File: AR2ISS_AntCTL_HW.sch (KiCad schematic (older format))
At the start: 2 parts

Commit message: started schematic
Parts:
- removed U?: STM32L522CCTx, Package_QFP:LQFP-48_7x7mm_P0.5mm, symbol AR2ISS:STM32L522CCTx
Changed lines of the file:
@@
 $Descr A4 11693 8268
 encoding utf-8
-Sheet 1 1
+Sheet 1 4
 Title ""
 Date ""
@@
 Comment4 ""
 $EndDescr
-$Comp
-L AR2ISS:STM32L522CCTx U?
-U 1 1 60612BC0
-P 5150 3100
-F 0 "U?" H 5150 1511 50  0000 C CNN
-F 1 "STM32L522CCTx" H 5150 1420 50  0000 C CNN
-F 2 "Package_QFP:LQFP-48_7x7mm_P0.5mm" H 4650 1700 50  0001 R CNN
-F 3 "http://www.st.com/st-web-https://www.st.com/resource/en/datasheet/stm32l552cc.pdf" H 5150 3100 50  0001 C CNN
-	1    5150 3100
-	1    0    0    -1
-$EndComp
 $Comp
 L Interface_Expansion:MCP23008-xSO U?
@@
 	1    0    0    -1
 $EndComp
+$Sheet
+S 1150 3750 900  950
+U 60660B68
+F0 "PowerSupply" 50
+F1 "PowerSupply.sch" 50
+F2 "ADC24V" I R 2050 3900 50
+F3 "ADC12V" I R 2050 4000 50
+F4 "ADCPWR" I R 2050 4100 50
+F5 "PREAMP_ON" I R 2050 4550 50
+$EndSheet
+$Sheet
+S 2550 2400 1650 2750
+U 606DDE00
+F0 "Microcontroller" 50
+F1 "Microcontroller.sch" 50
+F2 "I2C1_SCL" I R 4200 2550 50
+F3 "I2C1_SDA" I R 4200 2650 50
+F4 "I2C2_SCL" I R 4200 2800 50
+F5 "I2C2_SDA" I R 4200 2900 50
+F6 "USART1_TX" I R 4200 3100 50
+F7 "USART1_RX" I R 4200 3200 50
+F8 "SPI2_MOSI" I R 4200 3400 50
+F9 "SPI2_CLK" I R 4200 3500 50
+$EndSheet
+$Sheet
+S 5250 2550 700  950
+U 607267A8
+F0 "IOExpander" 50
+F1 "IOExpander.sch" 50
+$EndSheet
 $EndSCHEMATC

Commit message: added display pinout
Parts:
- removed U?: MCP23008-xSO, Package_SO:SOIC-18W_7.5x11.6mm_P1.27mm, symbol Interface_Expansion:MCP23008-xSO
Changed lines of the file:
@@
 $Descr A4 11693 8268
 encoding utf-8
-Sheet 1 4
+Sheet 1 6
 Title ""
 Date ""
@@
 Comment4 ""
 $EndDescr
-$Comp
-L Interface_Expansion:MCP23008-xSO U?
-U 1 1 60613912
-P 8050 2950
-F 0 "U?" H 8050 3731 50  0000 C CNN
-F 1 "MCP23008-xSO" H 8050 3640 50  0000 C CNN
-F 2 "Package_SO:SOIC-18W_7.5x11.6mm_P1.27mm" H 8050 1900 50  0001 C CNN
-F 3 "http://ww1.microchip.com/downloads/en/DeviceDoc/MCP23008-MCP23S08-Data-Sheet-20001919F.pdf" H 9350 1750 50  0001 C CNN
-	1    8050 2950
-	1    0    0    -1
-$EndComp
 $Sheet
 S 1150 3750 900  950
@@
 $EndSheet
 $Sheet
-S 5250 2550 700  950
+S 5700 2050 750  850
 U 607267A8
 F0 "IOExpander" 50
 F1 "IOExpander.sch" 50
+F2 "SDA" I L 5700 2100 50
+F3 "SCL" I L 5700 2200 50
+F4 "RESET" I L 5700 2450 50
+F5 "A0" I L 5700 2700 50
+F6 "A1" I L 5700 2800 50
+F7 "IOs" I R 6450 2250 50
 $EndSheet
+$Sheet
+S 5700 3200 750  850
+U 60679D69
+F0 "IOExpander2" 50
+F1 "IOExpander.sch" 50
+F2 "SDA" I L 5700 3250 50
+F3 "SCL" I L 5700 3350 50
+F4 "RESET" I L 5700 3600 50
+F5 "A0" I L 5700 3850 50
+F6 "A1" I L 5700 3950 50
+F7 "IOs" I R 6450 3400 50
+$EndSheet
+$Sheet
+S 6900 2000 950  2350
+U 60679DF6
+F0 "LCD" 50
+F1 "LCD.sch" 50
+F2 "ENC_A" I R 7850 2100 50
+F3 "ENC_B" I R 7850 2200 50
+F4 "DisplayData" I R 7850 2400 50
+F5 "DisplayCLK" I R 7850 2500 50
+F6 "LEDs" I L 6900 2250 50
+$EndSheet
+Wire Bus Line
+	6450 2250 6900 2250
 $EndSCHEMATC

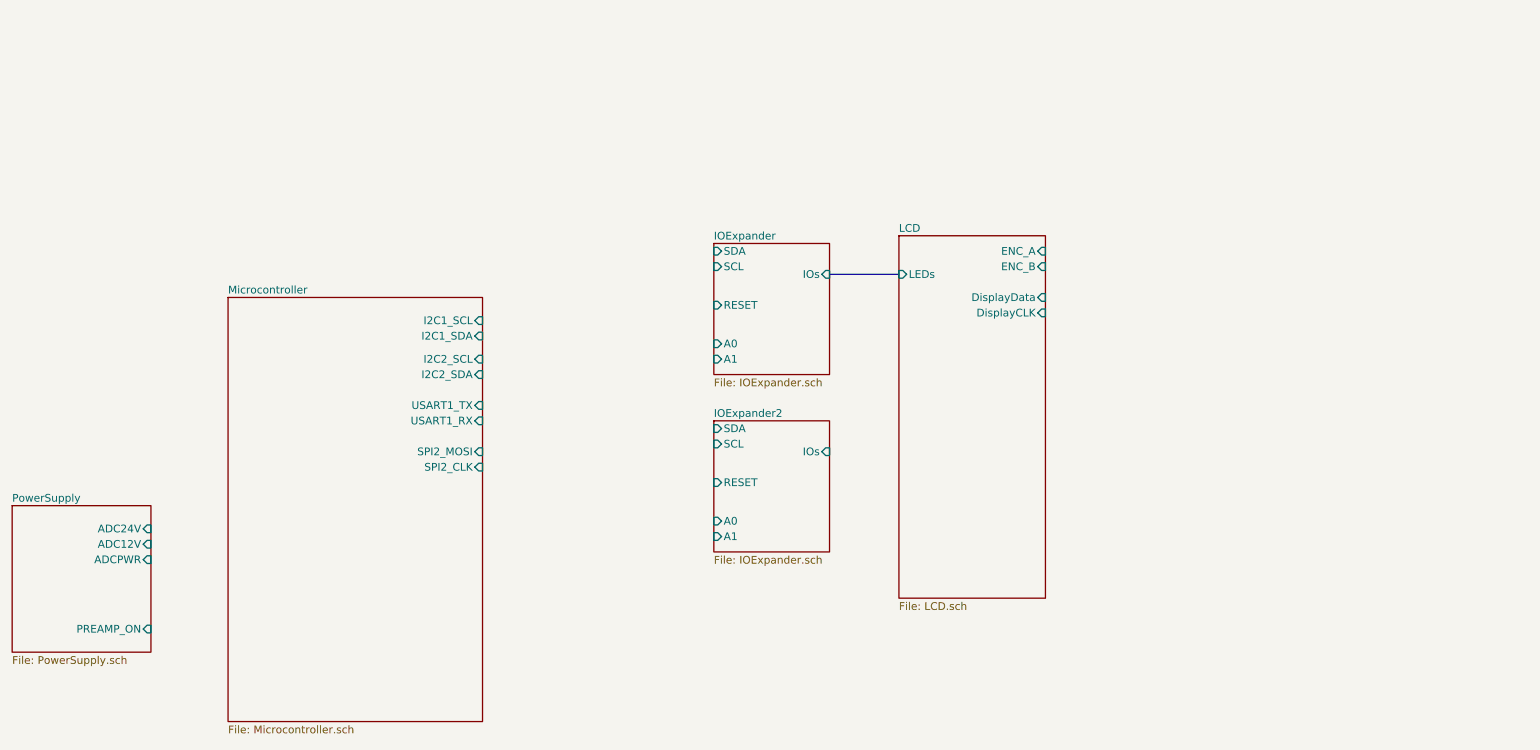
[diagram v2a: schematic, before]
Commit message: added rj45 input
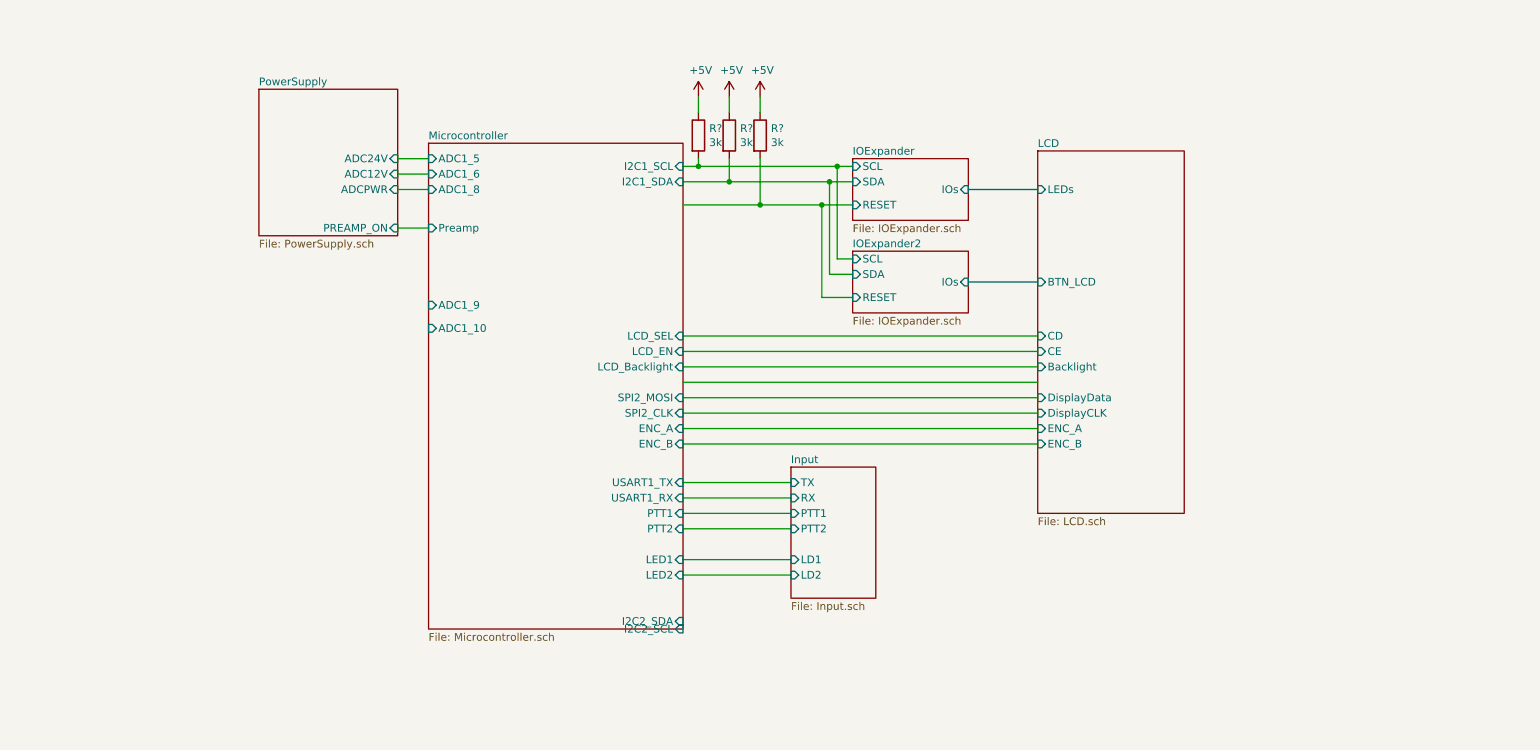
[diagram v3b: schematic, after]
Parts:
- added R? (x3): 3k, symbol AR2ISS:R
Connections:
- net labels added: +5V
- wire segments 0 -> 39

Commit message: Ready for layout
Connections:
- wire segments 39 -> 49
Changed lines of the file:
@@
 $Descr A4 11693 8268
 encoding utf-8
-Sheet 1 7
+Sheet 1 9
 Title ""
 Date ""
@@
 F4 "ADCPWR" I R 3650 1700 50
 F5 "PREAMP_ON" I R 3650 1950 50
-$EndSheet
-$Sheet
-S 3850 1400 1650 3150
-U 606DDE00
-F0 "Microcontroller" 50
-F1 "Microcontroller.sch" 50
-F2 "I2C1_SCL" I R 5500 1550 50
-F3 "I2C1_SDA" I R 5500 1650 50
-F4 "I2C2_SCL" I R 5500 4550 50
-F5 "I2C2_SDA" I R 5500 4500 50
-F6 "USART1_TX" I R 5500 3600 50
-F7 "USART1_RX" I R 5500 3700 50
-F8 "SPI2_MOSI" I R 5500 3050 50
-F9 "SPI2_CLK" I R 5500 3150 50
-F10 "LED1" I R 5500 4100 50
-F11 "LED2" I R 5500 4200 50
-F12 "ENC_A" I R 5500 3250 50
-F13 "ENC_B" I R 5500 3350 50
-F14 "PTT1" I R 5500 3800 50
-F15 "PTT2" I R 5500 3900 50
-F16 "LCD_EN" I R 5500 2750 50
-F17 "LCD_SEL" I R 5500 2650 50
-F18 "LCD_Backlight" I R 5500 2850 50
-F19 "ADC1_5" I L 3850 1500 50
-F20 "ADC1_6" I L 3850 1600 50
-F21 "ADC1_8" I L 3850 1700 50
-F22 "ADC1_9" I L 3850 2450 50
-F23 "ADC1_10" I L 3850 2600 50
-F24 "Preamp" I L 3850 1950 50
 $EndSheet
 $Sheet
@@
 Wire Wire Line
 	6000 1500 6000 1800
-Connection ~ 6000 1800
-Wire Wire Line
-	6000 1800 5500 1800
 $Comp
 L power:+5V #PWR?
@@
 Wire Wire Line
 	3650 1950 3850 1950
+$Sheet
+S 3850 1400 1650 3150
+U 606DDE00
+F0 "Microcontroller" 50
+F1 "Microcontroller.sch" 50
+F2 "I2C1_SCL" I R 5500 1550 50
+F3 "I2C1_SDA" I R 5500 1650 50
+F4 "USART1_TX" I R 5500 3600 50
+F5 "USART1_RX" I R 5500 3700 50
+F6 "SPI2_MOSI" I R 5500 3050 50
+F7 "SPI2_CLK" I R 5500 3150 50
+F8 "LED1" I R 5500 4100 50
+F9 "LED2" I R 5500 4200 50
+F10 "ENC_A" I R 5500 3250 50
+F11 "ENC_B" I R 5500 3350 50
+F12 "LCD_EN" I R 5500 2750 50
+F13 "LCD_SEL" I R 5500 2650 50
+F14 "LCD_Backlight" I R 5500 2850 50
+F15 "ADC1_5" I L 3850 1500 50
+F16 "ADC1_6" I L 3850 1600 50
+F17 "ADC1_8" I L 3850 1700 50
+F18 "ADC1_9" I L 3850 3900 50
+F19 "ADC1_10" I L 3850 4000 50
+F20 "Preamp" I L 3850 1950 50
+F21 "PTT_Main" I R 5500 3800 50
+F22 "PTT_Sub" I R 5500 3900 50
+F23 "ROT_UP" I L 3850 4150 50
+F24 "ROT_DOWN" I L 3850 4250 50
+F25 "ROT_LEFT" I L 3850 4350 50
+F26 "ROT_RIGHT" I L 3850 4450 50
+F27 "CREL_A" I L 3850 3300 50
+F28 "CREL_B" I L 3850 3200 50
+F29 "AMP" I L 3850 3000 50
+F30 "C_NO" I L 3850 2700 50
+F31 "C_NC" I L 3850 2800 50
+$EndSheet
+$Sheet
+S 2650 3850 750  950
+U 6074FD4F
+F0 "Rotor" 50
+F1 "Rotor.sch" 50
+F2 "ROT_UP" I R 3400 4150 50
+F3 "ROT_DOWN" I R 3400 4250 50
+F4 "ROT_LEFT" I R 3400 4350 50
+F5 "ROT_RIGHT" I R 3400 4450 50
+F6 "POT_ELE" I R 3400 3900 50
+F7 "POT_AZI" I R 3400 4000 50
+$EndSheet
+Wire Wire Line
+	3850 3900 3400 3900
+Wire Wire Line
+	3400 4000 3850 4000
+Wire Wire Line
+	3400 4150 3850 4150
+Wire Wire Line
+	3400 4250 3850 4250
+Wire Wire Line
+	3400 4350 3850 4350
+Wire Wire Line
+	3400 4450 3850 4450
+$Sheet
+S 2800 2600 600  800
+U 607E0323
+F0 "HF_Ctrl" 50
+F1 "HF_Ctrl.sch" 50
+F2 "AMP_ON" I R 3400 3000 50
+F3 "Coax_NO" I R 3400 2700 50
+F4 "Coax_NC" I R 3400 2800 50
+F5 "Coax_Rel_A" I R 3400 3200 50
+F6 "Coax_Ref_B" I R 3400 3300 50
+$EndSheet
+Wire Wire Line
+	3400 3000 3850 3000
+Wire Wire Line
+	3400 3200 3850 3200
+Wire Wire Line
+	3400 3300 3850 3300
+Wire Wire Line
+	3850 2700 3400 2700
+Wire Wire Line
+	3400 2800 3850 2800
 $EndSCHEMATC

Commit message: first layout
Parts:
- added U1, U2, U3, U4: non_plated, stmbl:non_plated_3mm, symbol stmbl:non_plated
- R1, R2, R3: renamed from R?; footprint (none) -> Resistor_SMD:R_0603_1608Metric
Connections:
- wire segments 49 -> 48
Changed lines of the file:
@@
 $Descr A4 11693 8268
 encoding utf-8
-Sheet 1 9
+Sheet 1 17
 Title ""
 Date ""
@@
 F0 "IOExpander2" 50
 F1 "IOExpander.sch" 50
-F2 "SDA" I L 6600 2250 50
+F2 "SDA" B L 6600 2250 50
 F3 "SCL" I L 6600 2150 50
 F4 "RESET" I L 6600 2400 50
-F5 "IOs" I R 7350 2300 50
+F5 "IO[0..15]" O R 7350 2300 50
 $EndSheet
 $Sheet
@@
 F4 "DisplayData" I L 7800 3050 50
 F5 "DisplayCLK" I L 7800 3150 50
-F6 "LEDs" I L 7800 1700 50
-F7 "BTN_LCD" I L 7800 2300 50
+F6 "LEDs[0..15]" I L 7800 1700 50
+F7 "BTN[0..15]" I L 7800 2300 50
 F8 "CD" I L 7800 2650 50
 F9 "CE" I L 7800 2750 50
@@
 AR Path="/60679D69/60A57B75" Ref="R?"  Part="1"
 AR Path="/607267A8/60A57B75" Ref="R?"  Part="1"
-AR Path="/60A57B75" Ref="R?"  Part="1"
-F 0 "R?" H 5670 1396 50  0000 L CNN
+AR Path="/60A57B75" Ref="R1"  Part="1"
+F 0 "R1" H 5670 1396 50  0000 L CNN
 F 1 "3k" H 5670 1305 50  0000 L CNN
-F 2 "" V 5530 1350 50  0001 C CNN
+F 2 "Resistor_SMD:R_0603_1608Metric" V 5530 1350 50  0001 C CNN
 F 3 "~" H 5600 1350 50  0001 C CNN
 	1    5600 1350
@@
 AR Path="/60679D69/60A57BD2" Ref="R?"  Part="1"
 AR Path="/607267A8/60A57BD2" Ref="R?"  Part="1"
-AR Path="/60A57BD2" Ref="R?"  Part="1"
-F 0 "R?" H 5870 1396 50  0000 L CNN
+AR Path="/60A57BD2" Ref="R2"  Part="1"
+F 0 "R2" H 5870 1396 50  0000 L CNN
 F 1 "3k" H 5870 1305 50  0000 L CNN
-F 2 "" V 5730 1350 50  0001 C CNN
+F 2 "Resistor_SMD:R_0603_1608Metric" V 5730 1350 50  0001 C CNN
 F 3 "~" H 5800 1350 50  0001 C CNN
 	1    5800 1350
@@
 AR Path="/607267A8/60A66FB9" Ref="#PWR?"  Part="1"
 AR Path="/60679D69/60A66FB9" Ref="#PWR?"  Part="1"
-AR Path="/60A66FB9" Ref="#PWR?"  Part="1"
-F 0 "#PWR?" H 5600 950 50  0001 C CNN
+AR Path="/60A66FB9" Ref="#PWR01"  Part="1"
+F 0 "#PWR01" H 5600 950 50  0001 C CNN
 F 1 "+5V" H 5615 1273 50  0000 C CNN
 F 2 "" H 5600 1100 50  0001 C CNN
@@
 AR Path="/607267A8/60A6763B" Ref="#PWR?"  Part="1"
 AR Path="/60679D69/60A6763B" Ref="#PWR?"  Part="1"
-AR Path="/60A6763B" Ref="#PWR?"  Part="1"
-F 0 "#PWR?" H 5800 950 50  0001 C CNN
+AR Path="/60A6763B" Ref="#PWR02"  Part="1"
+F 0 "#PWR02" H 5800 950 50  0001 C CNN
 F 1 "+5V" H 5815 1273 50  0000 C CNN
 F 2 "" H 5800 1100 50  0001 C CNN
@@
 Wire Wire Line
 	5800 1100 5800 1200
-$Sheet
-S 6200 3500 550  850
-U 60A6CF0D
-F0 "Input" 50
-F1 "Input.sch" 50
-F2 "TX" I L 6200 3600 50
-F3 "RX" I L 6200 3700 50
-F4 "PTT1" I L 6200 3800 50
-F5 "PTT2" I L 6200 3900 50
-F6 "LD1" I L 6200 4100 50
-F7 "LD2" I L 6200 4200 50
-$EndSheet
 Wire Wire Line
 	5500 3900 6200 3900
@@
 F0 "IOExpander" 50
 F1 "IOExpander.sch" 50
-F2 "SDA" I L 6600 1650 50
+F2 "SDA" B L 6600 1650 50
 F3 "SCL" I L 6600 1550 50
 F4 "RESET" I L 6600 1800 50
-F5 "IOs" I R 7350 1700 50
+F5 "IO[0..15]" O R 7350 1700 50
 $EndSheet
 Wire Wire Line
@@
 AR Path="/60679D69/60C11F73" Ref="R?"  Part="1"
 AR Path="/607267A8/60C11F73" Ref="R?"  Part="1"
-AR Path="/60C11F73" Ref="R?"  Part="1"
-F 0 "R?" H 6070 1396 50  0000 L CNN
+AR Path="/60C11F73" Ref="R3"  Part="1"
+F 0 "R3" H 6070 1396 50  0000 L CNN
 F 1 "3k" H 6070 1305 50  0000 L CNN
-F 2 "" V 5930 1350 50  0001 C CNN
+F 2 "Resistor_SMD:R_0603_1608Metric" V 5930 1350 50  0001 C CNN
 F 3 "~" H 6000 1350 50  0001 C CNN
 	1    6000 1350
@@
 AR Path="/607267A8/60C1252C" Ref="#PWR?"  Part="1"
 AR Path="/60679D69/60C1252C" Ref="#PWR?"  Part="1"
-AR Path="/60C1252C" Ref="#PWR?"  Part="1"
-F 0 "#PWR?" H 6000 950 50  0001 C CNN
+AR Path="/60C1252C" Ref="#PWR03"  Part="1"
+F 0 "#PWR03" H 6000 950 50  0001 C CNN
 F 1 "+5V" H 6015 1273 50  0000 C CNN
 F 2 "" H 6000 1100 50  0001 C CNN
@@
 	5500 2850 7800 2850
 Wire Wire Line
-	7800 2950 5500 2950
-Wire Wire Line
 	5500 3150 7800 3150
 Wire Wire Line
@@
 F0 "Microcontroller" 50
 F1 "Microcontroller.sch" 50
-F2 "I2C1_SCL" I R 5500 1550 50
-F3 "I2C1_SDA" I R 5500 1650 50
+F2 "I2C1_SCL" O R 5500 1550 50
+F3 "I2C1_SDA" B R 5500 1650 50
 F4 "USART1_TX" I R 5500 3600 50
 F5 "USART1_RX" I R 5500 3700 50
@@
 F15 "ADC1_5" I L 3850 1500 50
 F16 "ADC1_6" I L 3850 1600 50
-F17 "ADC1_8" I L 3850 1700 50
+F17 "ADC1_8" I L 3850 4000 50
 F18 "ADC1_9" I L 3850 3900 50
-F19 "ADC1_10" I L 3850 4000 50
+F19 "ADC1_10" I L 3850 1700 50
 F20 "Preamp" I L 3850 1950 50
 F21 "PTT_Main" I R 5500 3800 50
@@
 F1 "HF_Ctrl.sch" 50
 F2 "AMP_ON" I R 3400 3000 50
-F3 "Coax_NO" I R 3400 2700 50
-F4 "Coax_NC" I R 3400 2800 50
-F5 "Coax_Rel_A" I R 3400 3200 50
-F6 "Coax_Ref_B" I R 3400 3300 50
+F3 "Coax_NO" I R 3400 3300 50
+F4 "Coax_NC" I R 3400 3200 50
+F5 "Coax_Rel_A" I R 3400 2800 50
+F6 "Coax_Ref_B" I R 3400 2700 50
 $EndSheet
 Wire Wire Line
@@
 Wire Wire Line
 	3400 2800 3850 2800
+$Comp
+L stmbl:non_plated U1
+U 1 1 6070B730
+P 9350 700
+F 0 "U1" H 9528 753 60  0000 L CNN
+F 1 "non_plated" H 9528 647 60  0000 L CNN
+F 2 "stmbl:non_plated_3mm" H 9350 700 60  0001 C CNN
+F 3 "" H 9350 700 60  0001 C CNN
+	1    9350 700
+	1    0    0    -1
+$EndComp
+$Comp
+L stmbl:non_plated U3
+U 1 1 6070C63D
+P 10200 700
+F 0 "U3" H 10378 753 60  0000 L CNN
+F 1 "non_plated" H 10378 647 60  0000 L CNN
+F 2 "stmbl:non_plated_3mm" H 10200 700 60  0001 C CNN
+F 3 "" H 10200 700 60  0001 C CNN
+	1    10200 700
+	1    0    0    -1
+$EndComp
+$Comp
+L stmbl:non_plated U4
+U 1 1 6070CD54
+P 10200 1100
+F 0 "U4" H 10378 1153 60  0000 L CNN
+F 1 "non_plated" H 10378 1047 60  0000 L CNN
+F 2 "stmbl:non_plated_3mm" H 10200 1100 60  0001 C CNN
+F 3 "" H 10200 1100 60  0001 C CNN
+	1    10200 1100
+	1    0    0    -1
+$EndComp
+$Comp
+L stmbl:non_plated U2
+U 1 1 6070D205
+P 9350 1100
+F 0 "U2" H 9528 1153 60  0000 L CNN
+F 1 "non_plated" H 9528 1047 60  0000 L CNN
+F 2 "stmbl:non_plated_3mm" H 9350 1100 60  0001 C CNN
+F 3 "" H 9350 1100 60  0001 C CNN
+	1    9350 1100
+	1    0    0    -1
+$EndComp
+$Sheet
+S 6200 3500 550  850
+U 6072829D
+F0 "RS422" 50
+F1 "RS422.sch" 50
+F2 "TX" I L 6200 3600 50
+F3 "RX" I L 6200 3700 50
+F4 "LD1" I L 6200 4100 50
+F5 "LD2" I L 6200 4200 50
+F6 "PTT1" I L 6200 3800 50
+F7 "PTT2" I L 6200 3900 50
+$EndSheet
 $EndSCHEMATC

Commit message: uart rx tx reversed
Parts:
- U1, U2, U3, U4: symbol stmbl:non_plated -> AR2ISS_AntCTL_HW-rescue:non_plated-stmbl
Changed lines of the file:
@@
 	3400 2800 3850 2800
 $Comp
-L stmbl:non_plated U1
+L AR2ISS_AntCTL_HW-rescue:non_plated-stmbl U1
 U 1 1 6070B730
 P 9350 700
@@
 $EndComp
 $Comp
-L stmbl:non_plated U3
+L AR2ISS_AntCTL_HW-rescue:non_plated-stmbl U3
 U 1 1 6070C63D
 P 10200 700
@@
 $EndComp
 $Comp
-L stmbl:non_plated U4
+L AR2ISS_AntCTL_HW-rescue:non_plated-stmbl U4
 U 1 1 6070CD54
 P 10200 1100
@@
 $EndComp
 $Comp
-L stmbl:non_plated U2
+L AR2ISS_AntCTL_HW-rescue:non_plated-stmbl U2
 U 1 1 6070D205
 P 9350 1100
